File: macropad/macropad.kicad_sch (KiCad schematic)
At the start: 19 parts, among them U1 Arduino_Pro_Micro

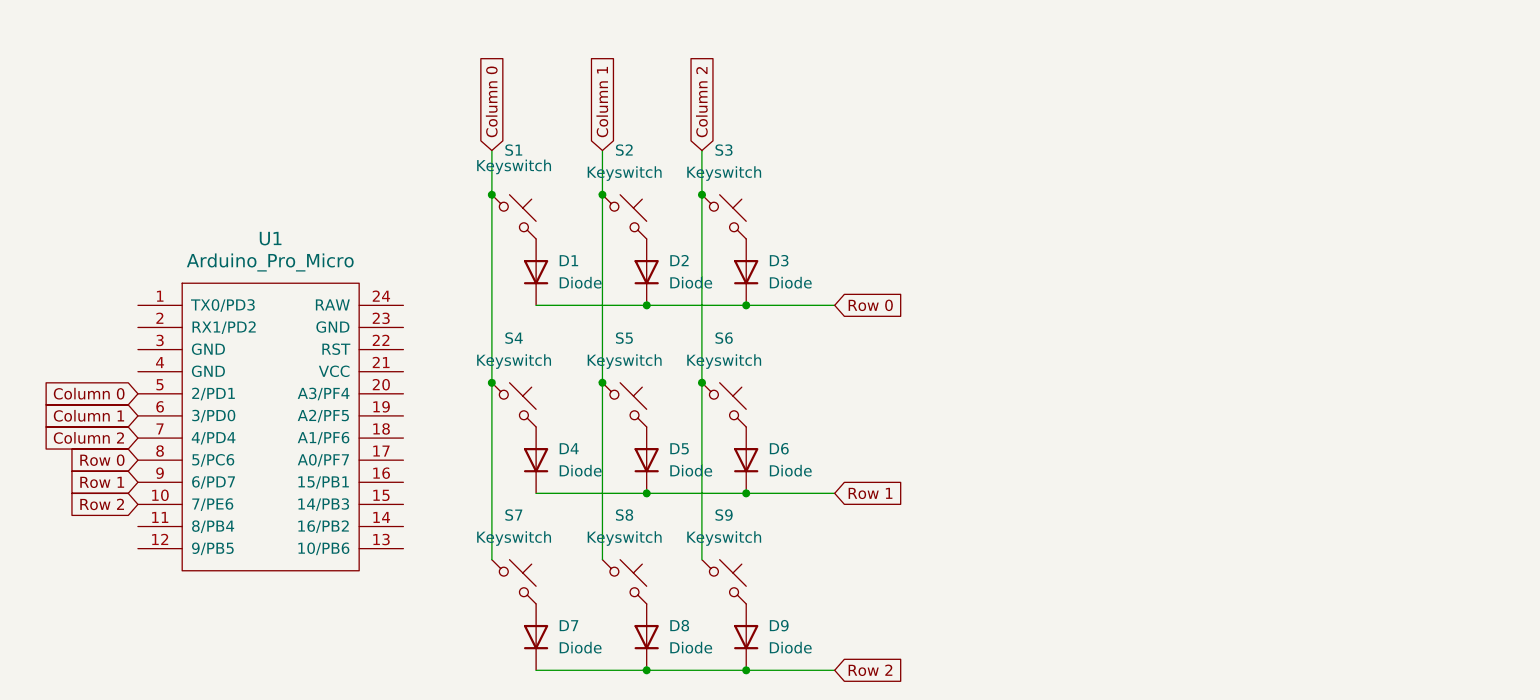
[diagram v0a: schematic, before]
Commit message: change pro micro to seeed studio xiao
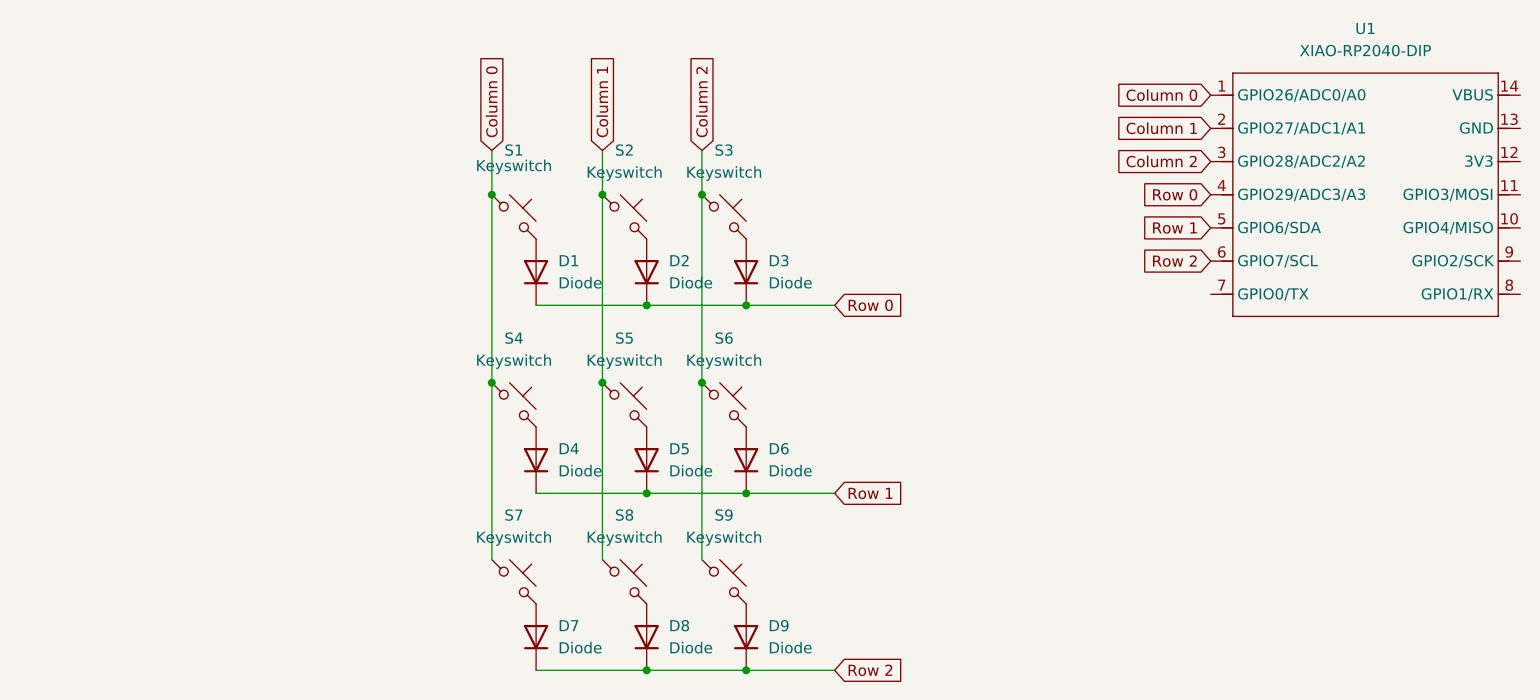
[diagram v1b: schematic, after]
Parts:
- removed U1: Arduino_Pro_Micro, ScottoKeebs_MCU:Arduino_Pro_Micro, symbol ScottoKeebs:MCU_Arduino_Pro_Micro
- added U1: XIAO-RP2040-DIP, OPL:XIAO-RP2040-DIP, symbol OPL:XIAO-RP2040-DIP
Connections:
- net Column 0: now also U1.1 (GPIO26/ADC0/A0)
- net Column 1: now also U1.2 (GPIO27/ADC1/A1)
- net Column 2: now also U1.3 (GPIO28/ADC2/A2)
- net Row 0: now also U1.4 (GPIO29/ADC3/A3)
- net Row 1: now also U1.5 (GPIO6/SDA)
- net Row 2: now also U1.6 (GPIO7/SCL)
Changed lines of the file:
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@@
 	(global_label "Row 1"
 		(shape input)
-		(at 52.07 105.41 180)
+		(at 175.26 76.2 180)
 		(fields_autoplaced yes)
 		(effects
@@
 		)
 		(property "Intersheetrefs" "${INTERSHEET_REFS}"
-			(at 43.1582 105.41 0)
+			(at 166.3482 76.2 0)
 			(effects
 				(font
@@
 	(global_label "Row 0"
 		(shape input)
-		(at 52.07 102.87 180)
+		(at 175.26 72.39 180)
 		(fields_autoplaced yes)
 		(effects
@@
 		)
 		(property "Intersheetrefs" "${INTERSHEET_REFS}"
-			(at 43.1582 102.87 0)
+			(at 166.3482 72.39 0)
 			(effects
 				(font
@@
 	(global_label "Column 0"
 		(shape input)
-		(at 52.07 95.25 180)
+		(at 175.26 60.96 180)
 		(fields_autoplaced yes)
 		(effects
@@
 		)
 		(property "Intersheetrefs" "${INTERSHEET_REFS}"
-			(at 39.8322 95.25 0)
+			(at 163.0222 60.96 0)
 			(effects
 				(font
@@
 	(global_label "Row 2"
 		(shape input)
-		(at 52.07 107.95 180)
+		(at 175.26 80.01 180)
 		(fields_autoplaced yes)
 		(effects
@@
 		)
 		(property "Intersheetrefs" "${INTERSHEET_REFS}"
-			(at 43.1582 107.95 0)
+			(at 166.3482 80.01 0)
 			(effects
 				(font
@@
 	(global_label "Column 1"
 		(shape input)
-		(at 52.07 97.79 180)
+		(at 175.26 64.77 180)
 		(fields_autoplaced yes)
 		(effects
@@
 		)
 		(property "Intersheetrefs" "${INTERSHEET_REFS}"
-			(at 39.8322 97.79 0)
+			(at 163.0222 64.77 0)
 			(effects
 				(font
@@
 	(global_label "Column 2"
 		(shape input)
-		(at 52.07 100.33 180)
+		(at 175.26 68.58 180)
 		(fields_autoplaced yes)
 		(effects
@@
 		)
 		(property "Intersheetrefs" "${INTERSHEET_REFS}"
-			(at 39.8322 100.33 0)
+			(at 163.0222 68.58 0)
 			(effects
 				(font
@@
 	)
 	(symbol
-		(lib_id "ScottoKeebs:MCU_Arduino_Pro_Micro")
-		(at 67.31 99.06 0)
-		(unit 1)
-		(exclude_from_sim no)
-		(in_bom yes)
-		(on_board yes)
-		(dnp no)
-		(fields_autoplaced yes)
-		(property "Reference" "U1"
-			(at 67.31 77.47 0)
-			(effects
-				(font
-					(size 1.524 1.524)
-				)
-			)
-		)
-		(property "Value" "Arduino_Pro_Micro"
-			(at 67.31 80.01 0)
-			(effects
-				(font
-					(size 1.524 1.524)
-				)
-			)
-		)
-		(property "Footprint" "ScottoKeebs_MCU:Arduino_Pro_Micro"
-			(at 67.31 121.92 0)
-			(effects
-				(font
-					(size 1.524 1.524)
-				)
-				(hide yes)
-			)
-		)
-		(property "Datasheet" ""
-			(at 93.98 162.56 90)
-			(effects
-				(font
-					(size 1.524 1.524)
-				)
-				(hide yes)
-			)
-		)
-		(property "Description" ""
-			(at 67.31 99.06 0)
-			(effects
-				(font
-					(size 1.27 1.27)
-				)
-				(hide yes)
-			)
-		)
-		(pin "4"
-		)
-		(pin "5"
-		)
-		(pin "6"
-		)
-		(pin "7"
-		)
-		(pin "8"
-		)
-		(pin "9"
-		)
-		(pin "10"
-		)
-		(pin "11"
-		)
-		(pin "12"
-		)
-		(pin "24"
-		)
-		(pin "23"
-		)
-		(pin "22"
-		)
-		(pin "21"
-		)
-		(pin "20"
-		)
-		(pin "19"
-		)
-		(pin "18"
-		)
-		(pin "17"
-		)
-		(pin "16"
-		)
-		(pin "15"
-		)
-		(pin "14"
-		)
-		(pin "13"
-		)
-		(pin "2"
-		)
-		(pin "1"
-		)
-		(pin "3"
-		)
-		(instances
-			(project ""
-				(path "/9e8fefbd-135f-4c75-8f1d-ab08dc8c9557"
-					(reference "U1")
-					(unit 1)
-				)
-			)
-		)
-	)
-	(symbol
 		(lib_id "ScottoKeebs:Placeholder_Keyswitch")
 		(at 95.25 96.52 0)
@@
 					(unit 1)
 				)
+			)
+		)
+	)
+	(symbol
+		(lib_id "OPL:XIAO-RP2040-DIP")
+		(at 179.07 55.88 0)
+		(unit 1)
+		(exclude_from_sim no)
+		(in_bom yes)
+		(on_board yes)
+		(dnp no)
+		(fields_autoplaced yes)
+		(property "Reference" "U1"
+			(at 193.04 53.34 0)
+			(effects
+				(font
+					(size 1.27 1.27)
+				)
+			)
+		)
+		(property "Value" "XIAO-RP2040-DIP"
+			(at 193.04 55.88 0)
+			(effects
+				(font
+					(size 1.27 1.27)
+				)
+			)
+		)
+		(property "Footprint" "OPL:XIAO-RP2040-DIP"
+			(at 193.548 88.138 0)
+			(effects
+				(font
+					(size 1.27 1.27)
+				)
+				(hide yes)
+			)
+		)
+		(property "Datasheet" ""
+			(at 179.07 55.88 0)
+			(effects
+				(font
+					(size 1.27 1.27)
+				)
+				(hide yes)
+			)
+		)
+		(property "Description" ""
+			(at 179.07 55.88 0)
+			(effects
+				(font
+					(size 1.27 1.27)
+				)
+				(hide yes)
+			)
+		)
+		(pin "1"
+		)
+		(pin "6"
+		)
+		(pin "7"
+		)
+		(pin "14"
+		)
+		(pin "13"
+		)
+		(pin "12"
+		)
+		(pin "11"
+		)
+		(pin "10"
+		)
+		(pin "9"
+		)
+		(pin "8"
+		)
+		(pin "4"
+		)
+		(pin "5"
+		)
+		(pin "3"
+		)
+		(pin "2"
+		)
+		(instances
+			(project ""
+				(path "/9e8fefbd-135f-4c75-8f1d-ab08dc8c9557"
+					(reference "U1")
+					(unit 1)
+				)
